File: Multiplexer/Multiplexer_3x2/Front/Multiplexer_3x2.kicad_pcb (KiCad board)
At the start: 2 copper layers, 15 x 128 mm, 3 parts

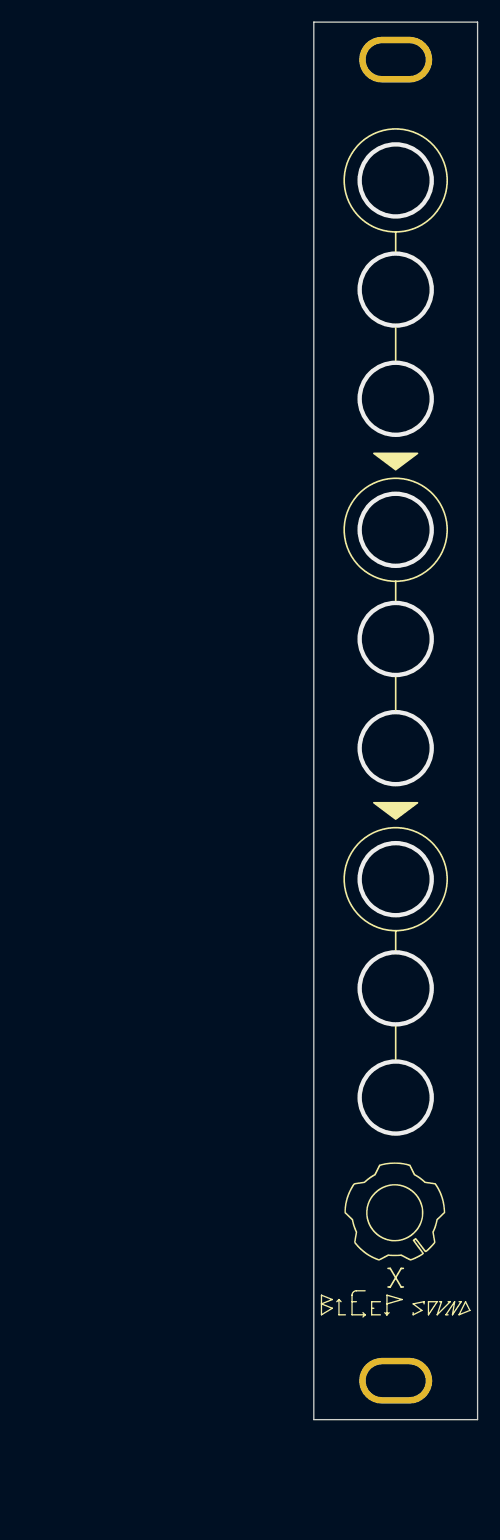
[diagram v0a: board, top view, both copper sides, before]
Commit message: fix position of mounting holes for front
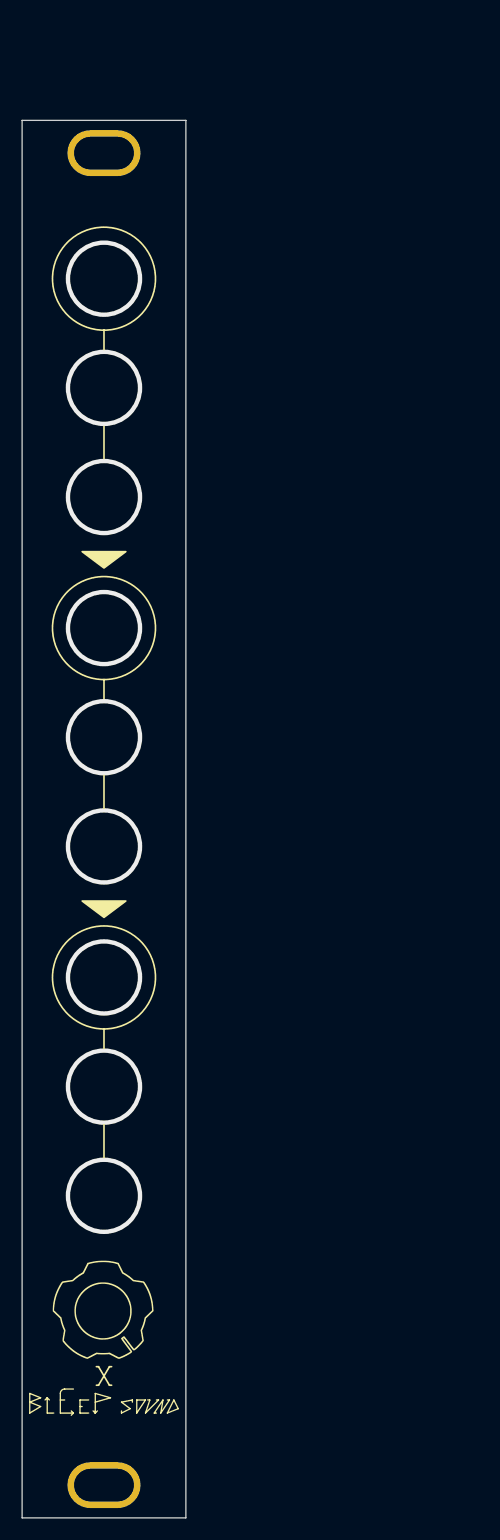
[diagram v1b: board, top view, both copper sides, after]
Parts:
- moved H1 28.4 mm to (55.3, 161.5)
- moved G*** 28.2 mm to (55.3, 145.5)
- moved H2 28.1 mm to (55.3, 39.5)

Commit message: Add iftec logo to multiplexer
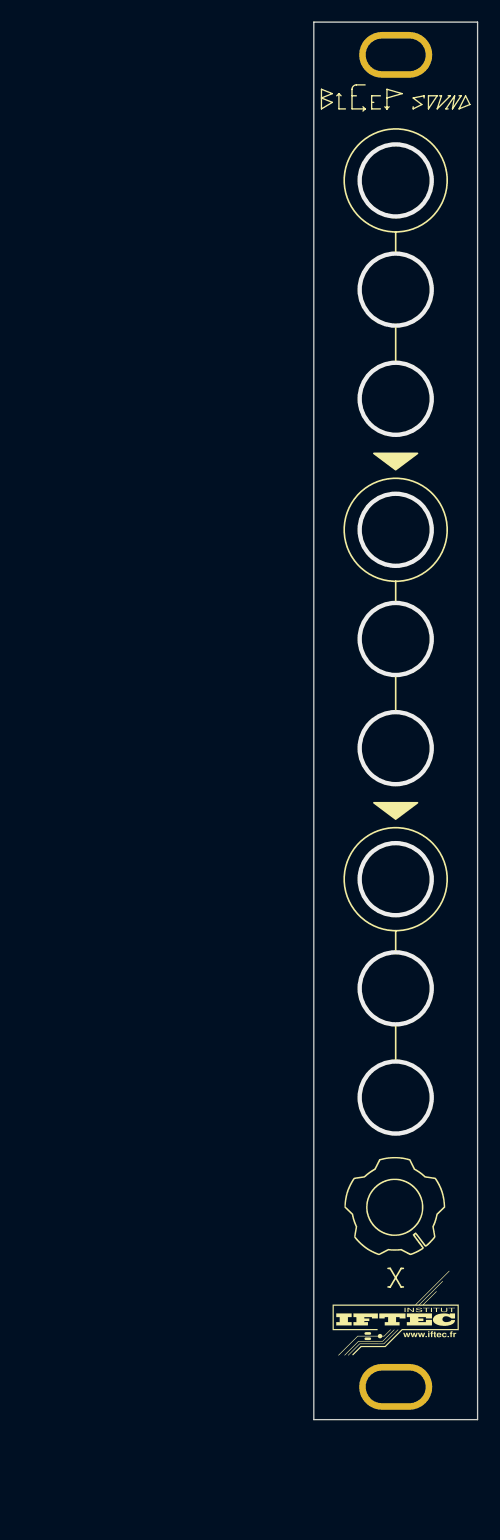
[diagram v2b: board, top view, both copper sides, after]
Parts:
- removed the G*** at (55.3, 145.5)
- added G***: LOGO, LOGO, F.Cu at (82.0, 136.0)
- added G***: LOGO, LOGO, F.Cu at (82.0, 145.8)
- moved H1 28.2 mm to (82.0, 152.5)
- moved H2 28.2 mm to (82.0, 30.5)
